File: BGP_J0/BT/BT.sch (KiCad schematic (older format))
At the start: 20 parts, among them P1 CONN_01X02, P2 CONN_01X02, P3 CONN_01X04, P4 CONN_01X04, Q1 MMBF5457

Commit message: Some Changes
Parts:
- C6: value 0.27u -> 0.47u
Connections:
- net RV_4: now also C4.2, RV3.1; no longer C5.2, RV3.3
- net RV_6: now also C5.2; no longer C4.2
- net RV_1 renamed RV_3
- net RV_3: now also RV3.3; no longer RV3.1
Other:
- moved on the sheet: C5, C6, R7
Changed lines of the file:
@@
 $EndComp
 $Comp
-L Earth #PWR4
+L Earth #PWR01
 U 1 1 5A6FCA5D
 P 4300 3900
-F 0 "#PWR4" H 4300 3650 50  0001 C CNN
+F 0 "#PWR01" H 4300 3650 50  0001 C CNN
 F 1 "Earth" H 4300 3750 50  0001 C CNN
 F 2 "" H 4300 3900 50  0000 C CNN
@@
 $EndComp
 $Comp
-L Earth #PWR5
+L Earth #PWR02
 U 1 1 5A6FCA7B
 P 5100 3900
-F 0 "#PWR5" H 5100 3650 50  0001 C CNN
+F 0 "#PWR02" H 5100 3650 50  0001 C CNN
 F 1 "Earth" H 5100 3750 50  0001 C CNN
 F 2 "" H 5100 3900 50  0000 C CNN
@@
 	5400 3100 5400 3050
 $Comp
-L VCC #PWR6
+L VCC #PWR03
 U 1 1 5A6FCE1E
 P 5400 3050
-F 0 "#PWR6" H 5400 2900 50  0001 C CNN
+F 0 "#PWR03" H 5400 2900 50  0001 C CNN
 F 1 "VCC" H 5400 3200 50  0000 C CNN
 F 2 "" H 5400 3050 50  0000 C CNN
@@
 L CP1_Small C5
 U 1 1 5A6FD2DA
-P 6400 3700
-F 0 "C5" H 6410 3770 50  0000 L CNN
-F 1 "1u" H 6410 3620 50  0000 L CNN
-F 2 "Capacitors_Tantalum_SMD:TantalC_SizeR_EIA-2012" H 6400 3700 50  0001 C CNN
-F 3 "" H 6400 3700 50  0000 C CNN
-	1    6400 3700
+P 6400 3650
+F 0 "C5" H 6410 3720 50  0000 L CNN
+F 1 "1u" H 6410 3570 50  0000 L CNN
+F 2 "Capacitors_Tantalum_SMD:TantalC_SizeR_EIA-2012" H 6400 3650 50  0001 C CNN
+F 3 "" H 6400 3650 50  0000 C CNN
+	1    6400 3650
 	0    -1   -1   0
 $EndComp
@@
 L CP1_Small C6
 U 1 1 5A6FD31E
-P 6400 4000
-F 0 "C6" H 6410 4070 50  0000 L CNN
-F 1 "0.27u" H 6410 3920 50  0000 L CNN
-F 2 "Capacitors_Tantalum_SMD:TantalC_SizeR_EIA-2012" H 6400 4000 50  0001 C CNN
-F 3 "" H 6400 4000 50  0000 C CNN
-	1    6400 4000
+P 6400 3950
+F 0 "C6" H 6410 4020 50  0000 L CNN
+F 1 "0.47u" H 6410 3870 50  0000 L CNN
+F 2 "Capacitors_Tantalum_SMD:TantalC_SizeR_EIA-2012" H 6400 3950 50  0001 C CNN
+F 3 "" H 6400 3950 50  0000 C CNN
+	1    6400 3950
 	0    -1   -1   0
 $EndComp
 $Comp
-L Earth #PWR8
+L Earth #PWR04
 U 1 1 5A6FD3C7
-P 6600 4350
-F 0 "#PWR8" H 6600 4100 50  0001 C CNN
-F 1 "Earth" H 6600 4200 50  0001 C CNN
-F 2 "" H 6600 4350 50  0000 C CNN
-F 3 "" H 6600 4350 50  0000 C CNN
-	1    6600 4350
+P 6600 4300
+F 0 "#PWR04" H 6600 4050 50  0001 C CNN
+F 1 "Earth" H 6600 4150 50  0001 C CNN
+F 2 "" H 6600 4300 50  0000 C CNN
+F 3 "" H 6600 4300 50  0000 C CNN
+	1    6600 4300
 	1    0    0    -1
 $EndComp
@@
 Connection ~ 6150 3350
 Wire Wire Line
-	6150 3600 6150 4000
-Wire Wire Line
-	6150 3700 6300 3700
-Wire Wire Line
-	6150 4000 6300 4000
-Connection ~ 6150 3700
-Wire Wire Line
-	6600 4100 6600 4000
-Wire Wire Line
-	6600 3700 6500 3700
+	6150 3650 6300 3650
+Wire Wire Line
+	6150 3950 6300 3950
+Connection ~ 6150 3650
+Wire Wire Line
+	6600 4050 6600 3950
+Wire Wire Line
+	6600 3650 6500 3650
 Wire Wire Line
 	6600 3350 6500 3350
-Text Label 6600 3700 0    60   ~ 0
+Text Label 6600 3350 0    60   ~ 0
 RV_4
-Text Label 6600 3350 0    60   ~ 0
+Text Label 6600 3650 0    60   ~ 0
 RV_6
 Text Label 7700 3850 0    60   ~ 0
@@
 Text Label 7250 3950 2    60   ~ 0
 RV_6
-Wire Wire Line
-	7250 3550 7250 3750
-Wire Wire Line
-	7250 3650 7700 3650
-Wire Wire Line
-	7700 3650 7700 3450
-Text Label 6600 4000 0    60   ~ 0
-RV_1
-Connection ~ 7250 3650
-Text Label 7250 3350 2    60   ~ 0
-RV_1
-Wire Wire Line
-	6600 4350 6600 4300
+Text Label 6600 3950 0    60   ~ 0
+RV_3
+Wire Wire Line
+	6600 4300 6600 4250
 Text Label 4300 3600 2    60   ~ 0
 IN
@@
 Vref
 $Comp
-L Earth #PWR10
+L Earth #PWR05
 U 1 1 5A6FE42E
 P 8250 3650
-F 0 "#PWR10" H 8250 3400 50  0001 C CNN
+F 0 "#PWR05" H 8250 3400 50  0001 C CNN
 F 1 "Earth" H 8250 3500 50  0001 C CNN
 F 2 "" H 8250 3650 50  0000 C CNN
@@
 $EndComp
 $Comp
-L VCC #PWR9
+L VCC #PWR06
 U 1 1 5A6FE538
 P 8250 3450
-F 0 "#PWR9" H 8250 3300 50  0001 C CNN
+F 0 "#PWR06" H 8250 3300 50  0001 C CNN
 F 1 "VCC" H 8250 3600 50  0000 C CNN
 F 2 "" H 8250 3450 50  0000 C CNN
@@
 IN_N
 $Comp
-L Earth #PWR1
+L Earth #PWR07
 U 1 1 5A6FE8A6
 P 3650 3400
-F 0 "#PWR1" H 3650 3150 50  0001 C CNN
+F 0 "#PWR07" H 3650 3150 50  0001 C CNN
 F 1 "Earth" H 3650 3250 50  0001 C CNN
 F 2 "" H 3650 3400 50  0000 C CNN
@@
 $EndComp
 $Comp
-L Earth #PWR2
+L Earth #PWR08
 U 1 1 5A6FE8EA
 P 3650 3900
-F 0 "#PWR2" H 3650 3650 50  0001 C CNN
+F 0 "#PWR08" H 3650 3650 50  0001 C CNN
 F 1 "Earth" H 3650 3750 50  0001 C CNN
 F 2 "" H 3650 3900 50  0000 C CNN
@@
 IN
 $Comp
-L Earth #PWR7
+L Earth #PWR09
 U 1 1 5A6FF586
 P 5400 4500
-F 0 "#PWR7" H 5400 4250 50  0001 C CNN
+F 0 "#PWR09" H 5400 4250 50  0001 C CNN
 F 1 "Earth" H 5400 4350 50  0001 C CNN
 F 2 "" H 5400 4500 50  0000 C CNN
@@
 L R_Small R7
 U 1 1 5A6FDA7A
-P 6600 4200
-F 0 "R7" H 6630 4220 50  0000 L CNN
-F 1 "1.8k" H 6630 4160 50  0000 L CNN
-F 2 "Resistors_SMD:R_0603_HandSoldering" H 6600 4200 50  0001 C CNN
-F 3 "" H 6600 4200 50  0000 C CNN
-	1    6600 4200
-	1    0    0    -1
-$EndComp
-Wire Wire Line
-	6600 4000 6500 4000
-$Comp
-L Earth #PWR3
+P 6600 4150
+F 0 "R7" H 6630 4170 50  0000 L CNN
+F 1 "1.8k" H 6630 4110 50  0000 L CNN
+F 2 "Resistors_SMD:R_0603_HandSoldering" H 6600 4150 50  0001 C CNN
+F 3 "" H 6600 4150 50  0000 C CNN
+	1    6600 4150
+	1    0    0    -1
+$EndComp
+Wire Wire Line
+	6600 3950 6500 3950
+$Comp
+L Earth #PWR010
 U 1 1 5A713616
 P 3650 4600
-F 0 "#PWR3" H 3650 4350 50  0001 C CNN
+F 0 "#PWR010" H 3650 4350 50  0001 C CNN
 F 1 "Earth" H 3650 4450 50  0001 C CNN
 F 2 "" H 3650 4600 50  0000 C CNN
@@
 	1    0    0    -1
 $EndComp
+Text Label 7250 3550 2    60   ~ 0
+RV_3
+Wire Wire Line
+	7700 3450 7700 3200
+Wire Wire Line
+	7700 3200 7200 3200
+Wire Wire Line
+	7200 3200 7200 3750
+Wire Wire Line
+	7200 3350 7250 3350
+Wire Wire Line
+	7200 3750 7250 3750
+Connection ~ 7200 3350
+Wire Wire Line
+	6150 3600 6150 3950
 $EndSCHEMATC

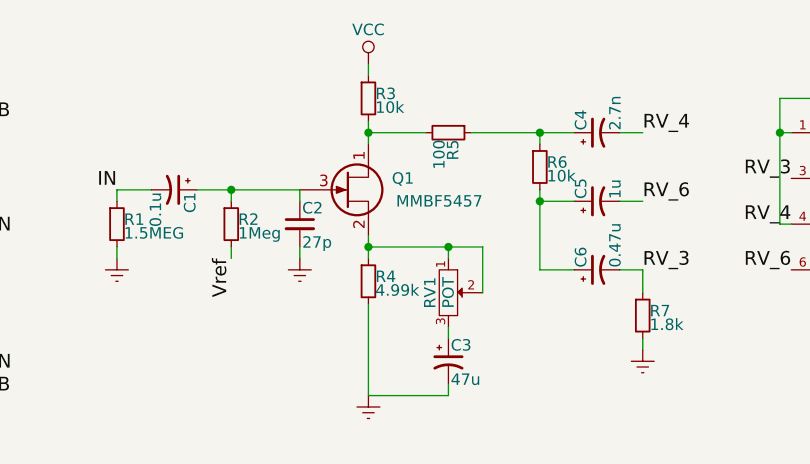
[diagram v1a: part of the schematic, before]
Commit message: J Amp changed for imrpoved distortion performance
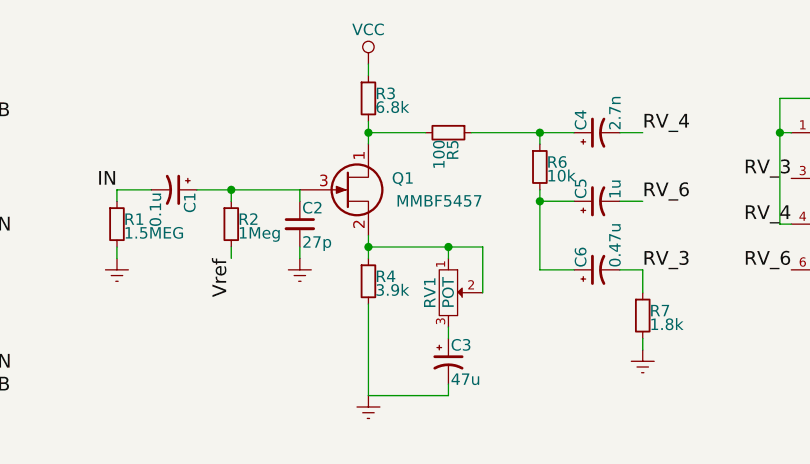
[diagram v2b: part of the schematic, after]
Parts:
- R3: value 10k -> 6.8k
- R4: value 4.99k -> 3.9k
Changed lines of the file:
@@
 P 5400 4000
 F 0 "R4" H 5430 4020 50  0000 L CNN
-F 1 "4.99k" H 5430 3960 50  0000 L CNN
+F 1 "3.9k" H 5430 3960 50  0000 L CNN
 F 2 "Resistors_SMD:R_0603_HandSoldering" H 5400 4000 50  0001 C CNN
 F 3 "" H 5400 4000 50  0000 C CNN
@@
 P 5400 3200
 F 0 "R3" H 5430 3220 50  0000 L CNN
-F 1 "10k" H 5430 3160 50  0000 L CNN
+F 1 "6.8k" H 5430 3160 50  0000 L CNN
 F 2 "Resistors_SMD:R_0603_HandSoldering" H 5400 3200 50  0001 C CNN
 F 3 "" H 5400 3200 50  0000 C CNN

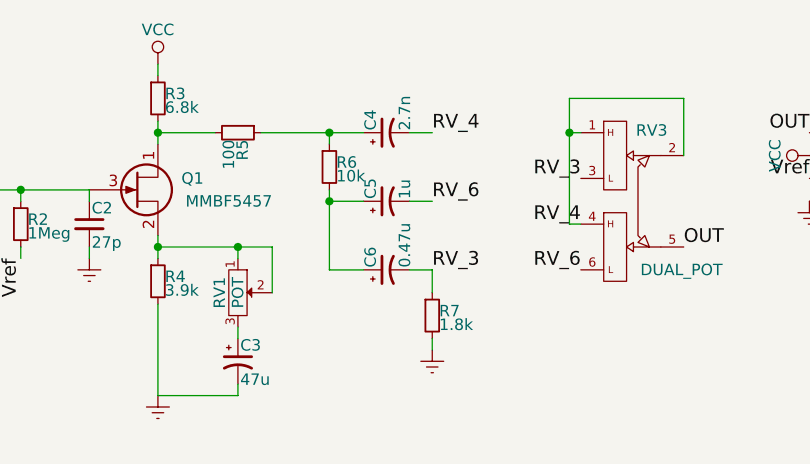
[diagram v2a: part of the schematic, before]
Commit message: J BT Cap changes
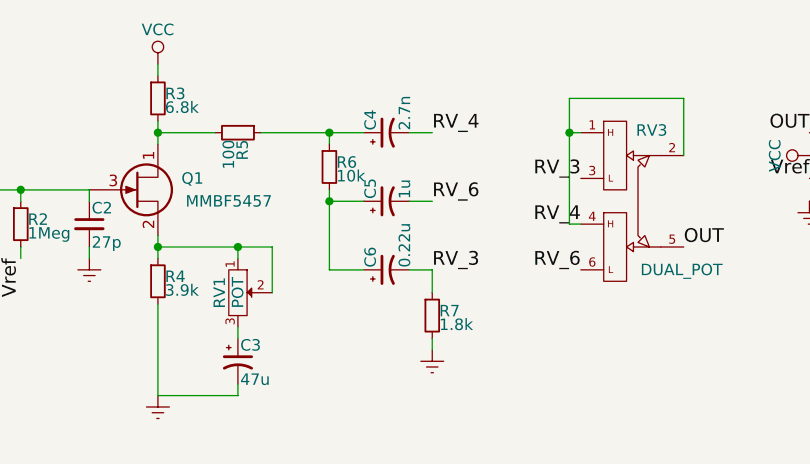
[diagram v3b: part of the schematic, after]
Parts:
- C4: footprint Capacitors_SMD:C_0603_HandSoldering -> Capacitors_SMD:C_0603
- C5: footprint Capacitors_Tantalum_SMD:TantalC_SizeR_EIA-2012 -> Capacitors_SMD:C_1210
- C6: value 0.47u -> 0.22u; footprint Capacitors_Tantalum_SMD:TantalC_SizeR_EIA-2012 -> Capacitors_SMD:C_1206
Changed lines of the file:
@@
 F 0 "C4" H 6410 3420 50  0000 L CNN
 F 1 "2.7n" H 6410 3270 50  0000 L CNN
-F 2 "Capacitors_SMD:C_0603_HandSoldering" H 6400 3350 50  0001 C CNN
+F 2 "Capacitors_SMD:C_0603" H 6400 3350 50  0001 C CNN
 F 3 "" H 6400 3350 50  0000 C CNN
 	1    6400 3350
@@
 F 0 "C5" H 6410 3720 50  0000 L CNN
 F 1 "1u" H 6410 3570 50  0000 L CNN
-F 2 "Capacitors_Tantalum_SMD:TantalC_SizeR_EIA-2012" H 6400 3650 50  0001 C CNN
+F 2 "Capacitors_SMD:C_1210" H 6400 3650 50  0001 C CNN
 F 3 "" H 6400 3650 50  0000 C CNN
 	1    6400 3650
@@
 P 6400 3950
 F 0 "C6" H 6410 4020 50  0000 L CNN
-F 1 "0.47u" H 6410 3870 50  0000 L CNN
-F 2 "Capacitors_Tantalum_SMD:TantalC_SizeR_EIA-2012" H 6400 3950 50  0001 C CNN
+F 1 "0.22u" H 6410 3870 50  0000 L CNN
+F 2 "Capacitors_SMD:C_1206" H 6400 3950 50  0001 C CNN
 F 3 "" H 6400 3950 50  0000 C CNN
 	1    6400 3950

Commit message: J BT Caps to film
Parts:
- C4: footprint Capacitors_SMD:C_0603 -> Capacitors_SMD:C_0805
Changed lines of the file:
@@
 F 0 "C4" H 6410 3420 50  0000 L CNN
 F 1 "2.7n" H 6410 3270 50  0000 L CNN
-F 2 "Capacitors_SMD:C_0603" H 6400 3350 50  0001 C CNN
+F 2 "Capacitors_SMD:C_0805" H 6400 3350 50  0001 C CNN
 F 3 "" H 6400 3350 50  0000 C CNN
 	1    6400 3350

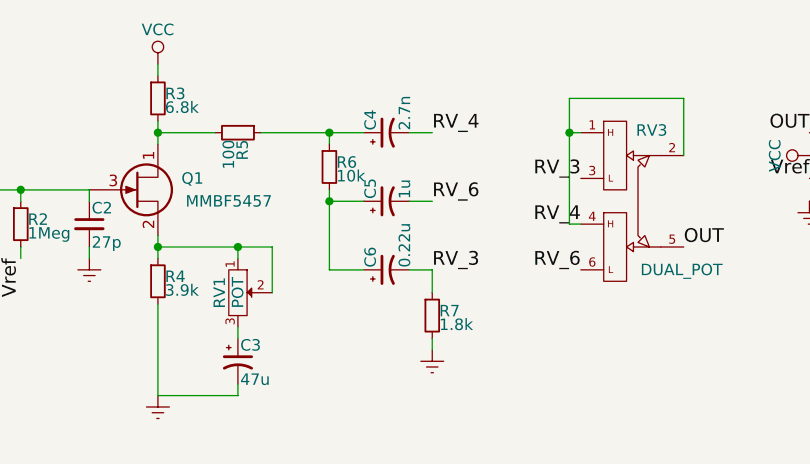
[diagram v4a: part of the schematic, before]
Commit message: Tone cap changed to female pin strip header for 0.047uF and 0.1uF
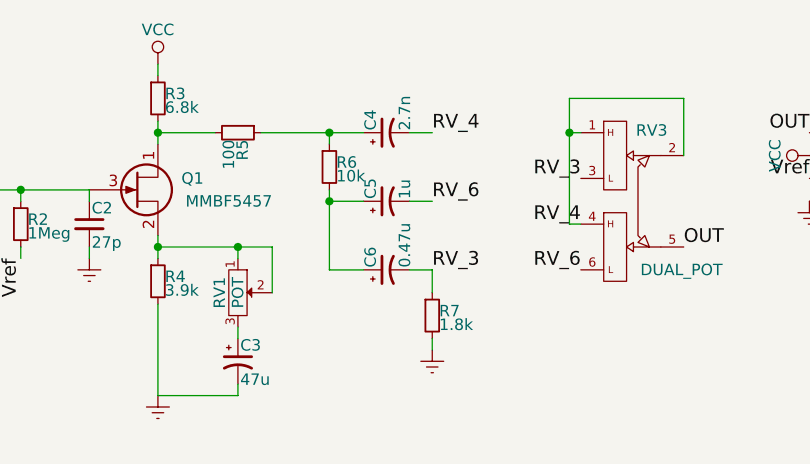
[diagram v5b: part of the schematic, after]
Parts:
- C6: value 0.22u -> 0.47u
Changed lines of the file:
@@
 P 6400 3950
 F 0 "C6" H 6410 4020 50  0000 L CNN
-F 1 "0.22u" H 6410 3870 50  0000 L CNN
+F 1 "0.47u" H 6410 3870 50  0000 L CNN
 F 2 "Capacitors_SMD:C_1206" H 6400 3950 50  0001 C CNN
 F 3 "" H 6400 3950 50  0000 C CNN

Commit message: J BT Pot wired incorrectly
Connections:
- net RV_6: now also C4.2; no longer C5.2
- net OUT renamed RV_5
- net RV_3 renamed RV_1
- net RV_1: now also RV3.1; no longer RV3.3
- net RV_4 renamed RV_2
- net RV_2: now also C5.2, RV3.3; no longer C4.2, RV3.1
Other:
- note added: "BASS"
- note added: "TREBLE"
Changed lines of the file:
@@
 Text Label 4800 3900 3    60   ~ 0
 Vref
-Wire Wire Line
-	4300 3900 4300 3850
-Wire Wire Line
-	4300 3650 4300 3600
-Wire Wire Line
-	4300 3600 4450 3600
-Wire Wire Line
-	4650 3600 5100 3600
-Wire Wire Line
-	4800 3600 4800 3650
-Wire Wire Line
-	5100 3600 5100 3650
-Connection ~ 4800 3600
 $Comp
 L Q_NJFET_DSG Q1
@@
 	1    0    0    -1
 $EndComp
-Wire Wire Line
-	4800 3900 4800 3850
-Wire Wire Line
-	5100 3900 5100 3850
 $Comp
 L R_Small R4
@@
 	1    0    0    -1
 $EndComp
-Wire Wire Line
-	5750 4450 5750 4500
-Wire Wire Line
-	5750 4500 5400 4500
-Wire Wire Line
-	5400 4500 5400 4100
-Wire Wire Line
-	5400 3900 5400 3800
-Wire Wire Line
-	5400 3850 5900 3850
-Wire Wire Line
-	5750 3850 5750 3900
-Connection ~ 5400 3850
-Wire Wire Line
-	5750 4200 5750 4250
-Wire Wire Line
-	5900 3850 5900 4050
-Connection ~ 5750 3850
-Wire Wire Line
-	5400 3400 5400 3300
-Wire Wire Line
-	5400 3100 5400 3050
 $Comp
 L VCC #PWR03
@@
 	0    1    1    0
 $EndComp
-Wire Wire Line
-	5650 3350 5400 3350
-Connection ~ 5400 3350
 $Comp
 L R_Small R6
@@
 $EndComp
 $Comp
-L DUAL_POT RV3
-U 1 1 5A6FD06A
-P 7400 3650
-F 0 "RV3" H 7560 3960 50  0000 C CNN
-F 1 "DUAL_POT" H 7690 3350 50  0000 C CNN
-F 2 "LIBS:Potentiometer_Alpha_Double_Vertical_Dual_Shaft" H 7400 3650 50  0001 C CNN
-F 3 "" H 7400 3650 50  0000 C CNN
-	1    7400 3650
-	1    0    0    -1
-$EndComp
-$Comp
 L CP1_Small C5
 U 1 1 5A6FD2DA
@@
 	1    0    0    -1
 $EndComp
-Wire Wire Line
-	5850 3350 6300 3350
-Wire Wire Line
-	6150 3350 6150 3400
-Connection ~ 6150 3350
-Wire Wire Line
-	6150 3650 6300 3650
-Wire Wire Line
-	6150 3950 6300 3950
-Connection ~ 6150 3650
-Wire Wire Line
-	6600 4050 6600 3950
-Wire Wire Line
-	6600 3650 6500 3650
-Wire Wire Line
-	6600 3350 6500 3350
-Text Label 6600 3350 0    60   ~ 0
-RV_4
-Text Label 6600 3650 0    60   ~ 0
-RV_6
-Text Label 7700 3850 0    60   ~ 0
-OUT
 Text Label 7250 3750 2    60   ~ 0
 RV_4
 Text Label 7250 3950 2    60   ~ 0
 RV_6
-Text Label 6600 3950 0    60   ~ 0
-RV_3
-Wire Wire Line
-	6600 4300 6600 4250
 Text Label 4300 3600 2    60   ~ 0
 IN
@@
 	0    -1   1    0
 $EndComp
-Text Label 8250 3350 2    60   ~ 0
-OUT
 $Comp
 L CONN_01X02 P1
@@
 	1    0    0    -1
 $EndComp
-Wire Wire Line
-	6600 3950 6500 3950
 $Comp
 L Earth #PWR010
@@
 Text Label 7250 3550 2    60   ~ 0
 RV_3
-Wire Wire Line
-	7700 3450 7700 3200
-Wire Wire Line
-	7700 3200 7200 3200
-Wire Wire Line
-	7200 3200 7200 3750
-Wire Wire Line
-	7200 3350 7250 3350
-Wire Wire Line
-	7200 3750 7250 3750
-Connection ~ 7200 3350
+Text Notes 7600 3550 0    60   ~ 0
+BASS
+Text Notes 7600 3950 0    60   ~ 0
+TREBLE
+Text Label 7700 3850 0    60   ~ 0
+RV_5
+Text Label 8250 3350 2    60   ~ 0
+RV_5
+Text Label 7700 3450 0    60   ~ 0
+RV_2
+Text Label 7250 3350 2    60   ~ 0
+RV_1
+$Comp
+L DUAL_POT RV3
+U 1 1 5A6FD06A
+P 7400 3650
+F 0 "RV3" H 7560 3960 50  0000 C CNN
+F 1 "DUAL_POT" H 7400 3250 50  0000 C CNN
+F 2 "LIBS:Potentiometer_Alpha_Double_Vertical_Dual_Shaft" H 7400 3650 50  0001 C CNN
+F 3 "" H 7400 3650 50  0000 C CNN
+	1    7400 3650
+	1    0    0    -1
+$EndComp
+Text Label 6600 3350 0    60   ~ 0
+RV_6
+Wire Wire Line
+	4300 3900 4300 3850
+Wire Wire Line
+	4300 3650 4300 3600
+Wire Wire Line
+	4300 3600 4450 3600
+Wire Wire Line
+	4650 3600 5100 3600
+Wire Wire Line
+	4800 3600 4800 3650
+Wire Wire Line
+	5100 3600 5100 3650
+Connection ~ 4800 3600
+Wire Wire Line
+	4800 3900 4800 3850
+Wire Wire Line
+	5100 3900 5100 3850
+Wire Wire Line
+	5750 4450 5750 4500
+Wire Wire Line
+	5750 4500 5400 4500
+Wire Wire Line
+	5400 4500 5400 4100
+Wire Wire Line
+	5400 3900 5400 3800
+Wire Wire Line
+	5400 3850 5900 3850
+Wire Wire Line
+	5750 3850 5750 3900
+Connection ~ 5400 3850
+Wire Wire Line
+	5750 4200 5750 4250
+Wire Wire Line
+	5900 3850 5900 4050
+Connection ~ 5750 3850
+Wire Wire Line
+	5400 3400 5400 3300
+Wire Wire Line
+	5400 3100 5400 3050
+Wire Wire Line
+	5650 3350 5400 3350
+Connection ~ 5400 3350
+Wire Wire Line
+	5850 3350 6300 3350
+Wire Wire Line
+	6150 3350 6150 3400
+Connection ~ 6150 3350
+Wire Wire Line
+	6150 3650 6300 3650
+Wire Wire Line
+	6150 3950 6300 3950
+Connection ~ 6150 3650
+Wire Wire Line
+	6600 4050 6600 3950
+Wire Wire Line
+	6600 3650 6500 3650
+Wire Wire Line
+	6600 3350 6500 3350
+Wire Wire Line
+	6600 4300 6600 4250
+Wire Wire Line
+	6600 3950 6500 3950
 Wire Wire Line
 	6150 3600 6150 3950
+Text Label 6600 3650 0    60   ~ 0
+RV_4
+Wire Wire Line
+	7250 3750 7250 3550
+Wire Wire Line
+	7250 3650 7700 3650
+Wire Wire Line
+	7700 3650 7700 3450
+Connection ~ 7250 3650
+Text Label 6600 3950 0    60   ~ 0
+RV_1
 $EndSCHEMATC

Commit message: J BT Changes from SMD film caps to THT
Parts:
- C5: footprint Capacitors_SMD:C_1210 -> Capacitor_THT:C_Rect_L4.6mm_W5.5mm_P2.50mm_MKS02_FKP02
- C6: footprint Capacitors_SMD:C_1206 -> Capacitor_THT:C_Rect_L4.6mm_W4.6mm_P2.50mm_MKS02_FKP02
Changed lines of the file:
@@
 F 0 "C5" H 6410 3720 50  0000 L CNN
 F 1 "1u" H 6410 3570 50  0000 L CNN
-F 2 "Capacitors_SMD:C_1210" H 6400 3650 50  0001 C CNN
+F 2 "Capacitor_THT:C_Rect_L4.6mm_W5.5mm_P2.50mm_MKS02_FKP02" H 6400 3650 50  0001 C CNN
 F 3 "" H 6400 3650 50  0000 C CNN
 	1    6400 3650
@@
 F 0 "C6" H 6410 4020 50  0000 L CNN
 F 1 "0.47u" H 6410 3870 50  0000 L CNN
-F 2 "Capacitors_SMD:C_1206" H 6400 3950 50  0001 C CNN
+F 2 "Capacitor_THT:C_Rect_L4.6mm_W4.6mm_P2.50mm_MKS02_FKP02" H 6400 3950 50  0001 C CNN
 F 3 "" H 6400 3950 50  0000 C CNN
 	1    6400 3950

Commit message: minor
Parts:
- C5: footprint Capacitor_THT:C_Rect_L4.6mm_W5.5mm_P2.50mm_MKS02_FKP02 -> Capacitors_THT:C_Rect_L4.6mm_W5.5mm_P2.50mm_MKS02_FKP02
- C6: footprint Capacitor_THT:C_Rect_L4.6mm_W4.6mm_P2.50mm_MKS02_FKP02 -> Capacitors_THT:C_Rect_L4.6mm_W4.6mm_P2.50mm_MKS02_FKP02
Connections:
- net Earth: now also P3.1 (P1); no longer P3.4 (P4)
- net IN: now also P3.4 (P4); no longer P3.1 (P1)
- net IN_B: now also P3.2 (P2); no longer P3.3 (P3)
- net IN_N: now also P3.3 (P3); no longer P3.2 (P2)
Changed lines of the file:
@@
 F 0 "C5" H 6410 3720 50  0000 L CNN
 F 1 "1u" H 6410 3570 50  0000 L CNN
-F 2 "Capacitor_THT:C_Rect_L4.6mm_W5.5mm_P2.50mm_MKS02_FKP02" H 6400 3650 50  0001 C CNN
+F 2 "Capacitors_THT:C_Rect_L4.6mm_W5.5mm_P2.50mm_MKS02_FKP02" H 6400 3650 50  0001 C CNN
 F 3 "" H 6400 3650 50  0000 C CNN
 	1    6400 3650
@@
 F 0 "C6" H 6410 4020 50  0000 L CNN
 F 1 "0.47u" H 6410 3870 50  0000 L CNN
-F 2 "Capacitor_THT:C_Rect_L4.6mm_W4.6mm_P2.50mm_MKS02_FKP02" H 6400 3950 50  0001 C CNN
+F 2 "Capacitors_THT:C_Rect_L4.6mm_W4.6mm_P2.50mm_MKS02_FKP02" H 6400 3950 50  0001 C CNN
 F 3 "" H 6400 3950 50  0000 C CNN
 	1    6400 3950
@@
 F 3 "" H 3450 4450 50  0000 C CNN
 	1    3450 4450
-	-1   0    0    -1
+	-1   0    0    1
 $EndComp
 $Comp
